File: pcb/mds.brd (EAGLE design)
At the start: 42.2 x 40 mm, 51 parts, among them IC1 MAX1555, Q1 CSTCR6M00G53Z, U2 ISD1900ISD1932, U5 ATMEGA328

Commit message: Code
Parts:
- R6: value (none) -> 56k
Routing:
- net CHG: track 22.9 -> 26.5 mm
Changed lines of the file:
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@@
 <attribute name="VALUE" x="4.445" y="27.94" size="1.27" layer="27" rot="R180"/>
 </element>
-<element name="R6" library="rcl" package="M0805" value="" x="31.75" y="12.065" smashed="yes" rot="R180">
+<element name="R6" library="rcl" package="M0805" value="56k" x="31.75" y="12.065" smashed="yes" rot="R180">
 <attribute name="NAME" x="30.1625" y="13.0175" size="0.8128" layer="25" rot="R180" align="top-right"/>
 <attribute name="VALUE" x="33.02" y="14.605" size="1.27" layer="27" rot="R180"/>
@@
 </element>
 <element name="C10" library="rcl" package="C0805" value="100nf" x="6.985" y="22.86" smashed="yes" rot="R180">
-<attribute name="NAME" x="7.62" y="21.9075" size="1.016" layer="25" rot="R180"/>
+<attribute name="NAME" x="6.6675" y="21.9075" size="1.016" layer="25" rot="R180"/>
 <attribute name="VALUE" x="8.255" y="25.4" size="1.27" layer="27" rot="R180"/>
 </element>
@@
 <wire x1="0.9525" y1="15.24" x2="0.9525" y2="10.795" width="0.254" layer="1"/>
 <wire x1="0.9525" y1="10.795" x2="1.5875" y2="10.16" width="0.254" layer="1"/>
-<wire x1="1.5875" y1="10.16" x2="6.985" y2="10.16" width="0.254" layer="1"/>
-<wire x1="6.985" y1="10.16" x2="8.255" y2="8.89" width="0.254" layer="1"/>
+<wire x1="1.5875" y1="10.16" x2="5.3975" y2="10.16" width="0.254" layer="1"/>
+<wire x1="5.3975" y1="10.16" x2="6.6675" y2="8.89" width="0.254" layer="1"/>
 <wire x1="12.3125" y1="12.2174" x2="12.3125" y2="11.36" width="0.254" layer="1"/>
 <wire x1="12.3125" y1="11.36" x2="12.065" y2="11.1125" width="0.254" layer="1"/>
@@
 <wire x1="31.4325" y1="24.13" x2="31.4325" y2="20.8675" width="0.254" layer="1"/>
 <wire x1="31.75" y1="21.36" x2="31.2025" y2="21.2725" width="0.254" layer="1"/>
-<wire x1="8.255" y1="8.89" x2="10.795" y2="8.89" width="0.254" layer="1"/>
+<wire x1="6.6675" y1="8.89" x2="10.795" y2="8.89" width="0.254" layer="1"/>
 <wire x1="10.795" y1="6.35" x2="11.1125" y2="6.0325" width="0.254" layer="1"/>
 <wire x1="17.145" y1="3.175" x2="17.145" y2="2.8575" width="0.254" layer="1"/>
@@
 <wire x1="14.9225" y1="24.7675" x2="15.8775" y2="24.7675" width="0.254" layer="1"/>
 <wire x1="15.8775" y1="24.7675" x2="16.1925" y2="25.0825" width="0.254" layer="1"/>
-<wire x1="16.1925" y1="25.0825" x2="16.1925" y2="27.6225" width="0.254" layer="1"/>
-<wire x1="16.1925" y1="27.6225" x2="14.9225" y2="29.5275" width="0.254" layer="1"/>
+<wire x1="16.1925" y1="25.0825" x2="16.1925" y2="28.2575" width="0.254" layer="1"/>
+<wire x1="16.1925" y1="28.2575" x2="14.9225" y2="29.5275" width="0.254" layer="1"/>
 <wire x1="22.86" y1="38.1" x2="22.86" y2="36.83" width="0.254" layer="16"/>
 <wire x1="22.86" y1="36.83" x2="22.225" y2="36.195" width="0.254" layer="16"/>
@@
 <wire x1="12.0625" y1="32.07" x2="9.525" y2="32.0675" width="0.254" layer="1"/>
 <wire x1="9.525" y1="32.0675" x2="8.5725" y2="31.115" width="0.254" layer="16"/>
-<wire x1="8.5725" y1="31.115" x2="8.5725" y2="13.6525" width="0.254" layer="16"/>
-<wire x1="8.3125" y1="12.2174" x2="8.3125" y2="13.3925" width="0.254" layer="1"/>
-<wire x1="8.3125" y1="13.3925" x2="8.5725" y2="13.6525" width="0.254" layer="1"/>
-<via x="8.5725" y="13.6525" extent="1-16" drill="0.6" diameter="1.016"/>
+<wire x1="8.5725" y1="31.115" x2="7.9375" y2="10.4775" width="0.254" layer="16"/>
+<wire x1="8.3125" y1="12.2174" x2="8.3125" y2="10.8525" width="0.254" layer="1"/>
+<wire x1="8.3125" y1="10.8525" x2="7.9375" y2="10.4775" width="0.254" layer="1"/>
+<via x="7.9375" y="10.4775" extent="1-16" drill="0.6" diameter="1.016"/>
 <via x="9.525" y="32.0675" extent="1-16" drill="0.6" diameter="1.016"/>
 </signal>

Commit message: Code !
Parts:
- removed BTN: Button, SparkFun:TACTILE_SWITCH_SMD
- removed MOT+, MOT-: (no value), wirepad:2,15/1,0
- removed RESET: Reset, SparkFun:TACTILE_SWITCH_SMD
- added ADC1, VIB+, VIB-: (no value), wirepad:1,6/0,8
- added C13: 100nf, rcl:C0805
- added R9: 4.7k, rcl:M0805
- added RST+, RST-: WIREPAD1,6/0,8, wirepad:1,6/0,8
- ADC0, LIPO+, LIPO-, MIC+, MIC-, PWR+, PWR-, SP+, SP-: device wirepad:2,15/1,0 -> wirepad:1,6/0,8
- moved ADC0 25.6 mm to (18.4, 47.9), turned to 0 degrees
- moved C10 21.6 mm to (12.1, 43.8)
- moved LIPO+ 0.63 mm to (13.7, 38.1)
- moved PWR+ 0.32 mm to (8.57, 38.1), turned to 0 degrees
- moved PWR- 0.32 mm to (6.67, 38.1), turned to 0 degrees
- moved SP+ 0.32 mm to (25.1, 1.91), turned to 0 degrees
- moved SP- 0.32 mm to (23.2, 1.91), turned to 0 degrees
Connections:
- new net ADC1: ADC1.1, C13.1, U5.22
- net ADC0: now also U5.19; no longer BTN.1, BTN.2, U5.23
- net CHG: now also R9.1
- net GND: now also C13.2, RST-.1; no longer BTN.3, BTN.4, RESET.1, RESET.2
- net M3: now also U5.23; no longer U5.19
- net M4: no longer U5.22
- net N$7: now also VIB-.1; no longer MOT-.1
- net RST: now also RST+.1; no longer RESET.3, RESET.4
- net VCC: now also R9.2, VIB+.1; no longer MOT+.1
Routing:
- net ADC0: track 29.5 -> 0.00 mm, vias 2 -> 0
- net RST: track 43.9 -> 33.0 mm, vias 1 -> 0
- net CHG: track 26.5 -> 28.7 mm
- net N$3: track 7.28 -> 5.03 mm
- net M4: track 26.5 -> 24.5 mm
- net N$7: track 3.24 -> 4.56 mm
- net N$2: track 7.01 -> 5.74 mm
- net M3: track 29.5 -> 28.5 mm
- net VCC: track 195.7 -> 194.9 mm
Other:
- board text added: "rev 0.x.x"
- board text removed: "rev 0.6.x"

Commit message: Code + Cad
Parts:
- removed Q1: CSTCR6M00G53Z, murata-filter:CSTCR6M
- added C14, C21, C22: 100nf, rcl:C0805
- added LED1: (no value), led:CHIP-LED0805
- added R10: 4.7k, rcl:M0805
- added U3: SF-BLUEGIGA_BLE112-A-VISUAL, ble112:SF-BLUEGIGA_BLE112-A
- moved BL 12.1 mm to (2.22, 21.0)
- moved RST- 4.13 mm to (6.03, 28.3)
- moved R8 3.19 mm to (6.35, 25.1)
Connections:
- removed net N$9: Q1.3, U5.8
- new net ??: U5.8
- new net LEDB: R10.2, U3.P0_0
- new net RX: U3.P0_5
- new net TX: U3.P0_4
- net GND: now also C14.1, C21.1, C22.1, LED1.C, U3.GND1, U3.GND2, U3.GND3, U3.GND4; no longer Q1.2
- net M4: now also U5.24
- net N$10: now also LED1.A, R10.1; no longer Q1.1, U5.7
- net VCC: now also C14.2, C21.2, C22.2, U3.AVDD1, U3.AVDD2, U3.DVDD, U3.VDD_USB
- net VIBRATOR: now also U5.7; no longer U5.24
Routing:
- net VCC: track 194.9 -> 150.7 mm
- net M3: track 28.5 -> 0.00 mm, vias 2 -> 0
- net M4: track 24.5 -> 0.00 mm, vias 2 -> 0
- net RST: track 33.0 -> 17.4 mm
- net DTR: track 14.8 -> 25.7 mm
- net TXO: track 6.80 -> 0.00 mm
- net RXI: track 5.15 -> 0.10 mm
- net N$9: track 4.34 -> 0.00 mm
- net N$10: track 4.04 -> 0.00 mm
- net CHG: track 28.7 -> 26.8 mm
- net VIBRATOR: track 19.2 -> 18.3 mm
- net GND: vias 10 -> 7

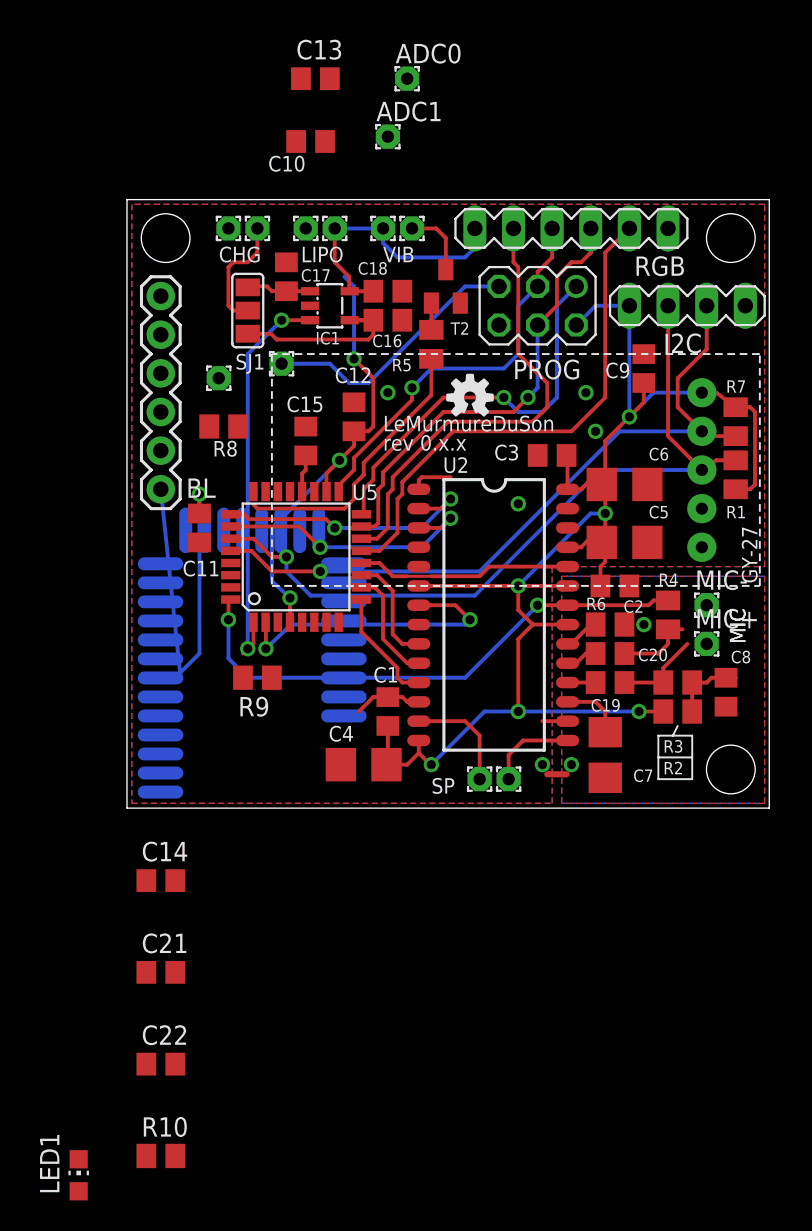
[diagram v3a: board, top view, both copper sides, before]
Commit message: PCB : Bluetooth module + enhancement
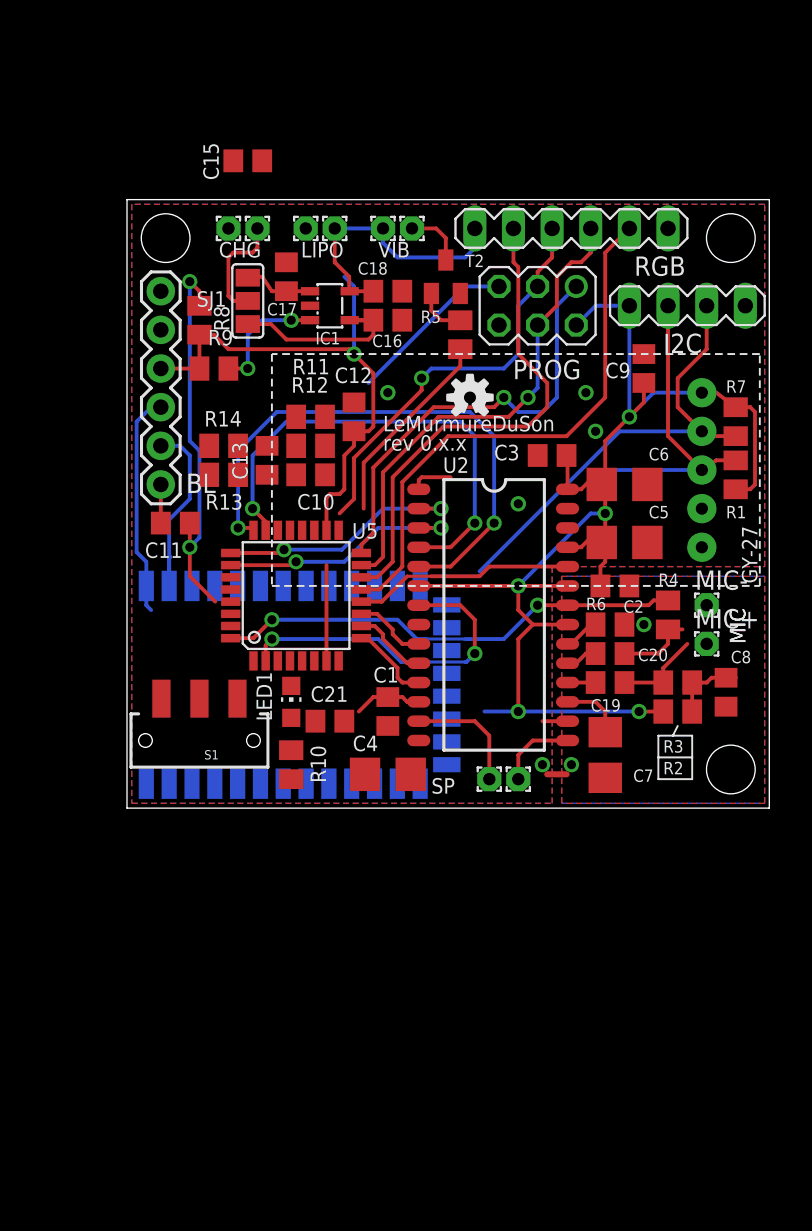
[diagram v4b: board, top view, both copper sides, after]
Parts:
- removed ADC0, ADC1: (no value), wirepad:1,6/0,8
- removed C14, C22: 100nf, rcl:C0805
- removed RST+, RST-: WIREPAD1,6/0,8, wirepad:1,6/0,8
- removed U3: SF-BLUEGIGA_BLE112-A-VISUAL, ble112:SF-BLUEGIGA_BLE112-A
- added R11, R12, R13, R14: ??, rcl:M0805
- added S1: (no value), SparkFun-Electromechanical:SWITCH-SPDT-SMD
- added U1: HC_06, Bluetooth HC-05:BLUETOOTH_SMD
- moved LED1 34.1 mm to (10.8, 6.99)
- moved R10 27.1 mm to (10.8, 2.86), turned to 270 degrees
- moved C13 25.3 mm to (9.21, 22.9), turned to 90 degrees
- moved C10 21.9 mm to (12.1, 21.9)
- moved R9 20.5 mm to (5.71, 28.9), turned to 180 degrees
- moved C21 19.9 mm to (13.3, 5.71)
- moved C15 18.8 mm to (7.94, 42.5), turned to 0 degrees
- moved R8 7.16 mm to (4.76, 32.1), turned to 270 degrees
- moved U5 2.54 mm to (11.1, 14.0)
- moved R5 2.01 mm to (21.9, 31.1)
- moved C4 1.71 mm to (17.1, 2.22)
- moved C11 1.62 mm to (3.17, 18.7), turned to 0 degrees
- moved SP+ 0.64 mm to (25.7, 1.91)
- moved SP- 0.64 mm to (23.8, 1.91)
- moved SJ1 0.63 mm to (7.94, 33.3)
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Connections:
- removed net ??: U5.8
- removed net ADC0: ADC0.1, C10.1, U5.19
- removed net ADC1: ADC1.1, C13.1, U5.22
- removed net RX: U3.P0_5
- removed net TX: U3.P0_4
- new net AD0: C10.1, R11.1, R12.2, U5.19
- new net AD1: C13.1, R13.1, R14.2, U5.22
- new net KEY: S1.2, U1.26
- net GND: now also R12.1, R14.1, S1.3, U1.13, U1.21, U1.22; no longer C14.1, C22.1, RST-.1, U3.GND1, U3.GND2, U3.GND3, U3.GND4
- net LEDB: now also U1.24, U5.8; no longer U3.P0_0
- net N$8: now also R13.2
- net RST: no longer RST+.1
- net RXI: now also U1.1
- net TXO: now also U1.2
- net VCC: now also R11.2, S1.1, U1.12; no longer C14.2, C22.2, U3.AVDD1, U3.AVDD2, U3.DVDD, U3.VDD_USB
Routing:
- net M4: track 0.00 -> 36.6 mm, vias 0 -> 2
- net M3: track 0.00 -> 31.2 mm, vias 0 -> 2
- net SDA: track 50.6 -> 20.8 mm, vias 1 -> 0
- net DTR: track 25.7 -> 2.54 mm, vias 1 -> 0
- net RST: track 17.4 -> 36.9 mm, vias 0 -> 2
- net CHG: track 26.8 -> 8.04 mm
- net SCL: track 47.4 -> 30.5 mm, vias 1 -> 0
- net RXI: track 0.10 -> 14.8 mm
- net TXO: track 0.00 -> 13.2 mm
- net VCC: track 150.7 -> 144.5 mm, vias 9 -> 6
- net LED: track 35.8 -> 31.1 mm
- net MOSI: track 29.4 -> 32.0 mm
- net SS: track 30.2 -> 32.8 mm
- net M7: track 7.51 -> 4.97 mm
- net SI: track 33.7 -> 36.3 mm
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
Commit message: PCB
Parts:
- moved C15 21.3 mm to (8.26, 21.3)
- moved LED1 6.30 mm to (6.03, 2.86), turned to 90 degrees
- moved S1 4.51 mm to (1.91, 7.94), turned to 90 degrees
- moved C21 2.88 mm to (10.5, 6.03)
- moved C13 2.54 mm to (9.21, 25.4)
- moved R13 1.59 mm to (6.35, 23.5)
- moved R14 1.59 mm to (6.35, 25.4)
- moved C12 0.90 mm to (15.6, 26.4)
- moved SP- 0.64 mm to (24.4, 1.91)
- moved R10 0.63 mm to (10.2, 2.86), turned to 0 degrees
- moved SP+ 0.63 mm to (26.4, 1.91)
- moved C10 0.32 mm to (12.1, 22.2), turned to 0 degrees
- moved C11 0.32 mm to (3.17, 18.4)
- moved R11 0.32 mm to (12.1, 26.0), turned to 0 degrees
- moved R12 0.32 mm to (12.1, 24.1), turned to 180 degrees
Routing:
- net CHG: track 8.04 -> 42.4 mm
- net VCC: track 144.5 -> 176.7 mm, vias 6 -> 9
- net SDA: track 20.8 -> 51.0 mm, vias 0 -> 2
- net SCL: track 30.5 -> 59.8 mm, vias 0 -> 1
- net LEDB: track 0.00 -> 14.2 mm, vias 0 -> 1
- net KEY: track 0.00 -> 13.9 mm, vias 0 -> 1
- net N$8: track 7.38 -> 21.2 mm, vias 0 -> 2
- net AD1: track 0.00 -> 10.5 mm, vias 0 -> 2
- net RST: track 36.9 -> 45.8 mm
- net AD0: track 0.00 -> 8.27 mm
- net RXI: track 14.8 -> 20.8 mm, vias 0 -> 1
- net TXO: track 13.2 -> 18.2 mm, vias 0 -> 1
- net VIBRATOR: track 19.4 -> 24.1 mm
- net AREF: track 0.00 -> 4.53 mm
- net N$3: track 5.03 -> 7.28 mm
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
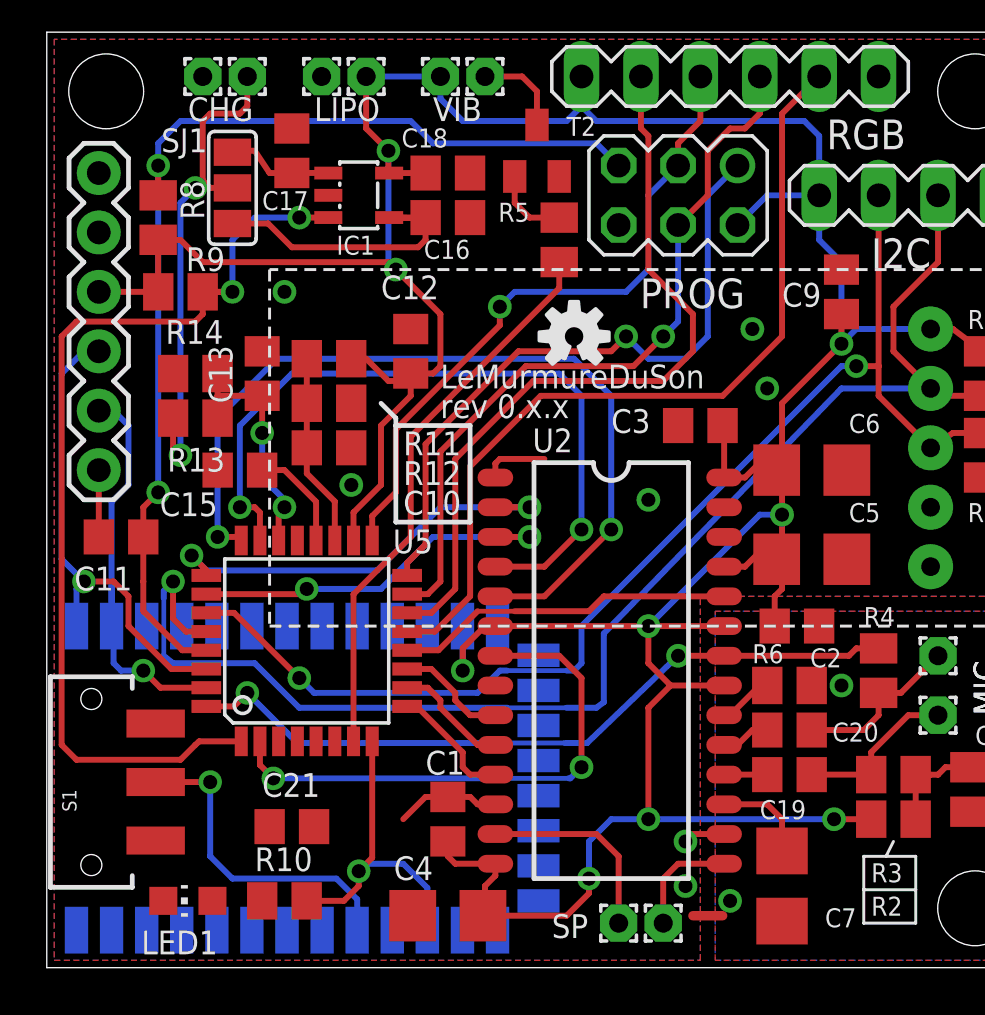
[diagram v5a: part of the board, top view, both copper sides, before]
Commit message: Stl file + PCB
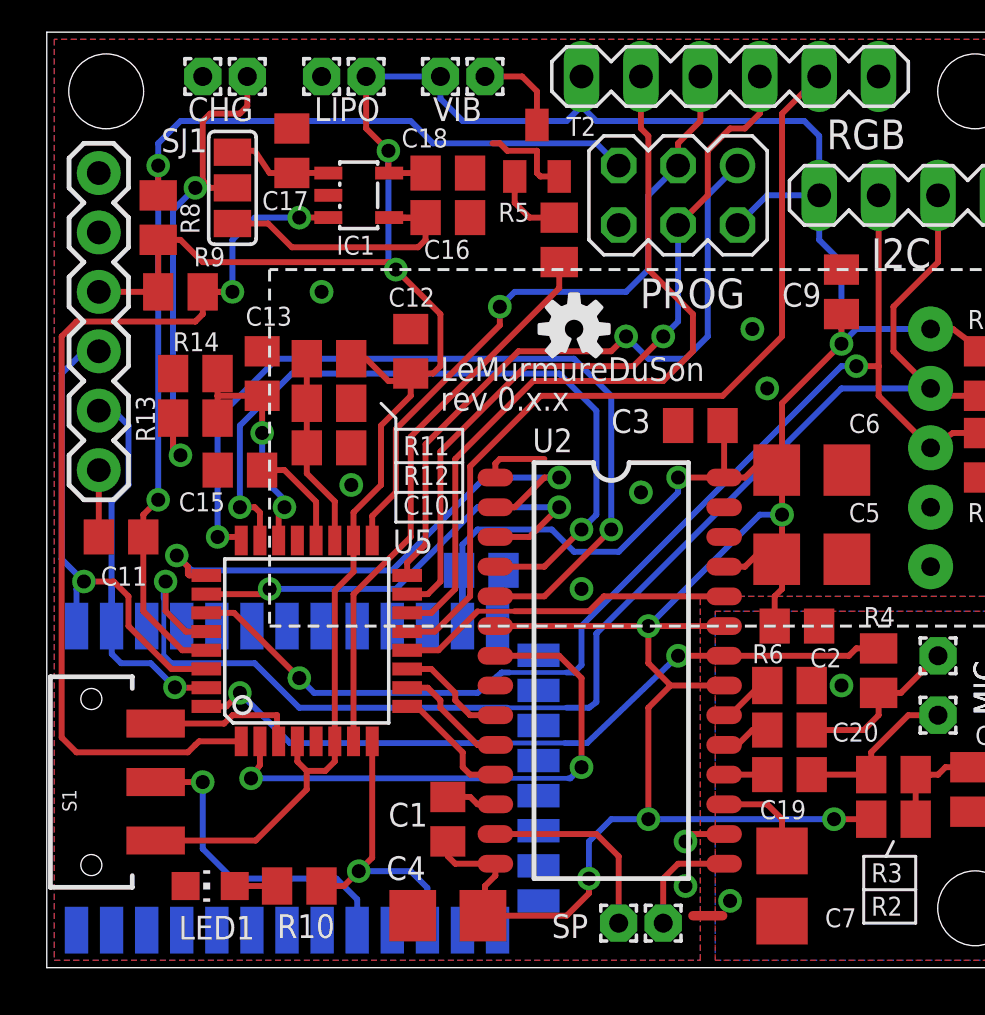
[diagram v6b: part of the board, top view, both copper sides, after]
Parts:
- moved C21 13.6 mm to (18.6, 17.0), flipped to the bottom
- moved LED1 1.14 mm to (6.99, 3.49)
- moved R10 0.90 mm to (10.8, 3.49)
- moved U$14 0.32 mm to (22.5, 27.3)
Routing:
- net VCC: track 176.7 -> 212.2 mm
- net GND: track 10.2 -> 18.3 mm, vias 9 -> 10
- net M1: track 18.4 -> 23.3 mm
- net M2: track 16.3 -> 19.9 mm
- net N$10: track 0.00 -> 1.81 mm
- net LEDB: track 14.2 -> 12.7 mm
- net M5: track 23.1 -> 23.9 mm
- net M3: track 31.6 -> 32.1 mm

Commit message: PCB 0.8.0
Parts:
- removed LED1: (no value), led:CHIP-LED0805
- added LED: (no value), led:CHIP-LED0805
- added SJ2, SJ3: (no value), jumper:SJ_2
- BLUETOOTH: value HC_06 -> HC_0x
- moved R10 3.43 mm to (7.94, 1.59)
- moved MIC+ 0.95 mm to (39.1, 10.8)
- moved MIC- 0.95 mm to (39.1, 13.3)
- moved BL 0.32 mm to (2.22, 21.0)
- moved C19 0.32 mm to (32.1, 8.26)
- moved C20 0.32 mm to (32.1, 10.2)
- moved C8 0.32 mm to (39.7, 7.62)
- moved R6 0.32 mm to (32.1, 12.1)
- moved S1 0.32 mm to (1.91, 8.26)
- moved R9 0.32 mm to (5.71, 28.6)
- moved R4 0.32 mm to (35.9, 12.7)
- renumbered U1 to BLUETOOTH
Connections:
- removed net KEY: BLUETOOTH.26, S1.2
- new net HC05_KEY: BLUETOOTH.34, SJ2.3
- new net HC05_LED: BLUETOOTH.32, SJ3.3
- new net HC06_KEY: BLUETOOTH.26, SJ2.1
- new net HC06_LED: BLUETOOTH.24, SJ3.1
- new net N$4: S1.2, SJ2.2
- net GND: now also LED.C; no longer LED1.C
- net LEDB: now also SJ3.2; no longer BLUETOOTH.24
- net N$10: now also LED.A; no longer LED1.A
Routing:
- net GND: track 18.3 -> 34.2 mm, vias 10 -> 16
- net KEY: track 13.7 -> 0.00 mm, vias 1 -> 0
- net HC05_KEY: track 0.00 -> 13.0 mm, vias 0 -> 1
- net N$4: track 0.00 -> 10.0 mm, vias 0 -> 2
- net HC06_LED: track 0.00 -> 7.94 mm, vias 0 -> 1
- net HC06_KEY: track 0.00 -> 6.60 mm, vias 0 -> 1
- net HC05_LED: track 0.00 -> 4.77 mm, vias 0 -> 1
- net LEDB: track 12.7 -> 15.7 mm, vias 1 -> 2
- net M5: track 23.9 -> 26.6 mm
- net N$3: track 7.28 -> 8.54 mm
- net N$1: track 2.37 -> 3.06 mm
- net N$2: track 7.01 -> 7.65 mm
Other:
- board text added: "hugo, 09/2013"
- board text added: "rev 0.8.0"
- board text removed: "SPEAKER"
- board text removed: "hugo, 07/2013"
- board text removed: "rev 0.x.x"
